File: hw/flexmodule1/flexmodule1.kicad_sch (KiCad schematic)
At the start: 62 parts, among them J1 AudioJack2, J2 AudioJack2, J3 AudioJack2, J4 AudioJack2, J5 AudioJack2, J6 rack_power, J7 SWD, J8 USB_B_Micro, J9 jack, SW1 mode, SW2 bootloader, U1 STM32G431K6Tx, U2 ADP7142AUJZ-5.0, U4 ADP7142AUJZ-3.3, U6 74HCT541, Y1 Crystal

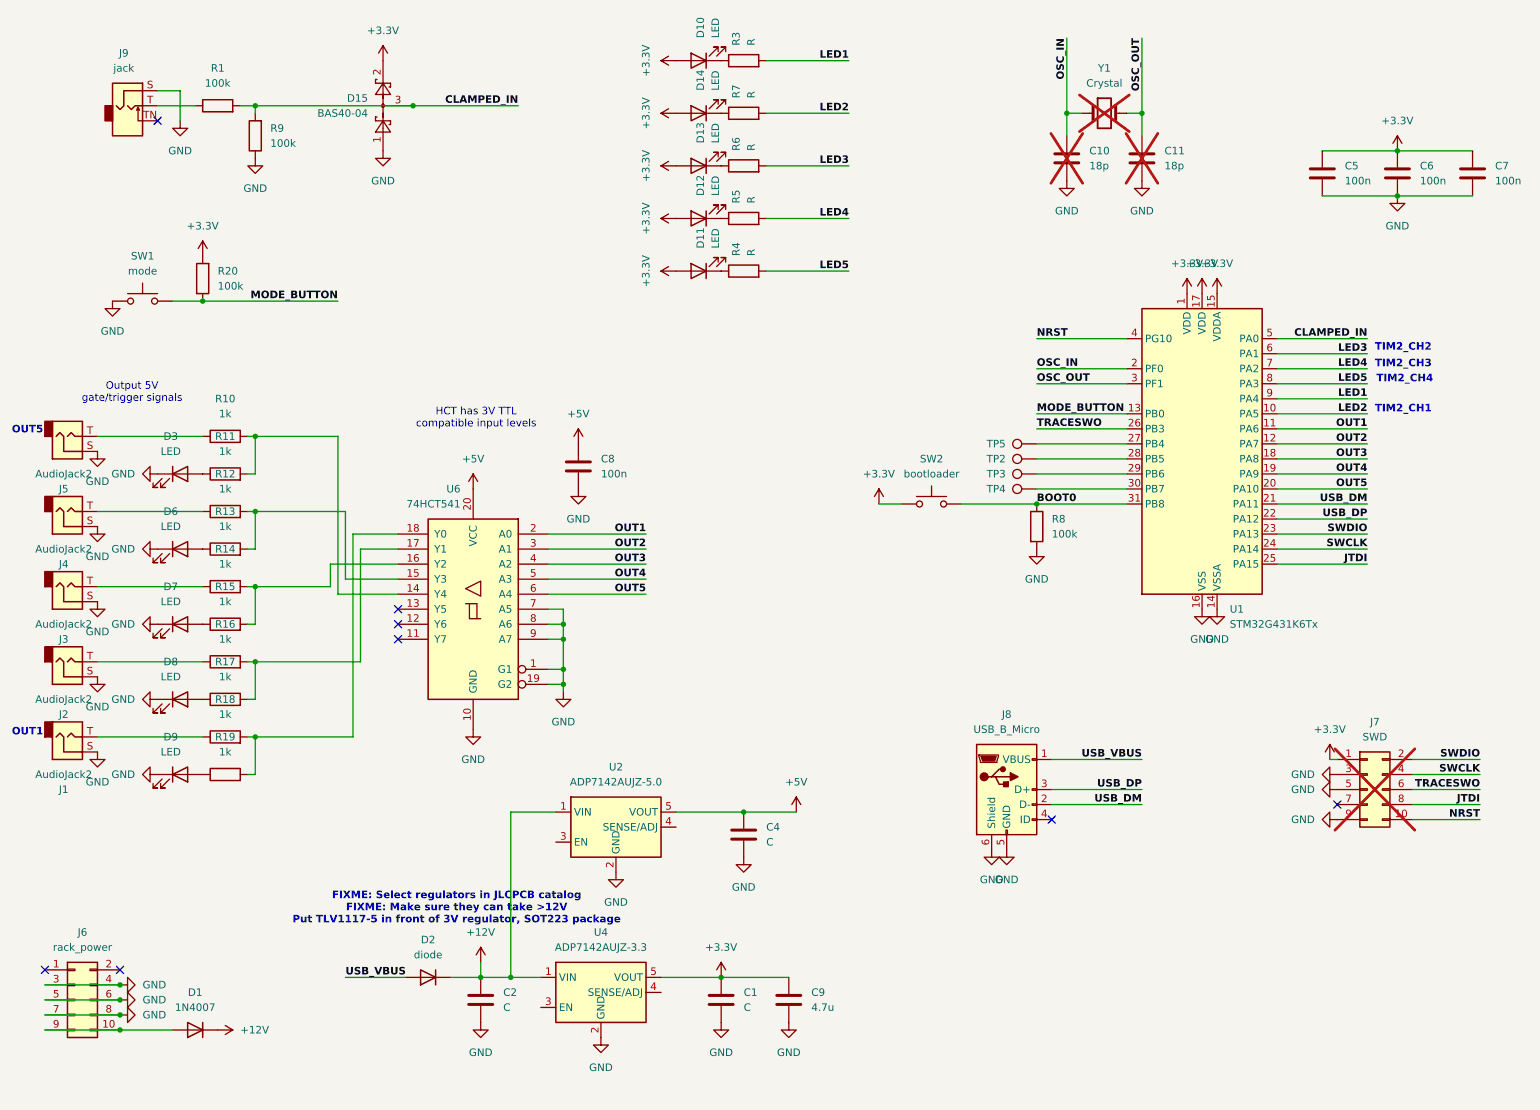
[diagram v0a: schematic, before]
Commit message: Change to a bigger LDO
Use a bigger 5V regulator with 12V input tolerance, so it might be
able to dissipate more heat. Not sure how warm this is going to get.
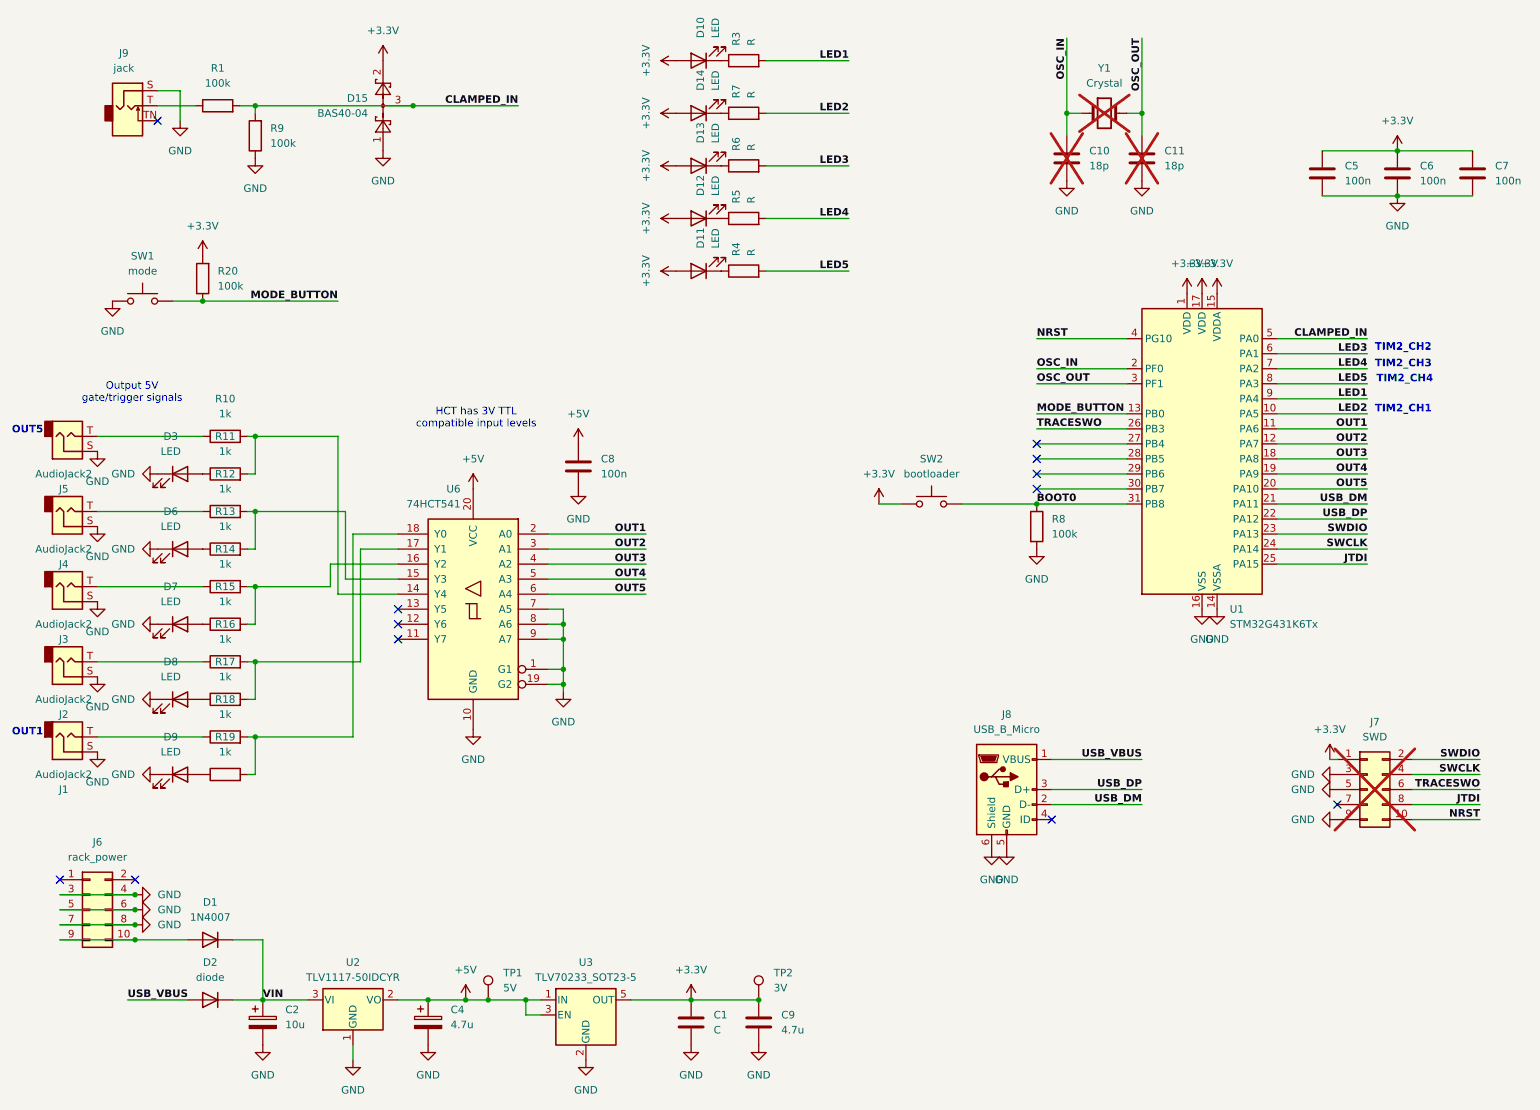
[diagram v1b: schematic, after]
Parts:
- removed TP3, TP4, TP5: tp, Holes:TP_0.9mm, symbol Connector:TestPoint
- removed U2: ADP7142AUJZ-5.0, Package_TO_SOT_SMD:TSOT-23-5, symbol Regulator_Linear:ADP7142AUJZ-5.0
- removed U4: ADP7142AUJZ-3.3, Package_TO_SOT_SMD:TSOT-23-5, symbol Regulator_Linear:ADP7142AUJZ-3.3
- added TP1: 5V, Holes:TP_0.9mm, symbol Connector:TestPoint
- added U2: TLV1117-50IDCYR, Package_TO_SOT_SMD:SOT-223-3_TabPin2, symbol Regulator_Linear:TLV1117-50
- added U3: TLV70233_SOT23-5, Package_TO_SOT_SMD:SOT-23-5, symbol Regulator_Linear:TLV70233_SOT23-5
- C2: value C -> 10u; footprint Capacitor_SMD:C_0603_1608Metric_Pad1.08x0.95mm_HandSolder -> Capacitor_THT:CP_Radial_D5.0mm_P2.50mm; symbol Device:C -> Device:C_Polarized
- C4: value C -> 4.7u; footprint Capacitor_SMD:C_0603_1608Metric_Pad1.08x0.95mm_HandSolder -> Capacitor_SMD:C_1206_3216Metric_Pad1.33x1.80mm_HandSolder; symbol Device:C -> Device:C_Polarized
- SW2: footprint Button_Switch_THT:SW_PUSH_6mm -> Button_Switch_SMD:SW_SPST_B3S-1000
- TP2: value tp -> 3V
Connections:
- net +3.3V: now also TP2.1, U3.5 (OUT)
- net +5V: now also TP1.1, U2.2 (VO), U3.1 (IN), U3.3 (EN)
- net GND: now also U2.1 (GND), U3.2 (GND)
- net at U1.28 (PB5): no longer TP2.1
- net +12V renamed VIN
- net VIN: now also U2.3 (VI)
- no-connect marks 8 -> 12
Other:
- note removed: "FIXME: Select regulators in JLCPCB catalog FIXME: Make sure they can take >12V Put TLV1117-5 in front of 3V regulator, SOT223 package"
- moved on the sheet: C1, C9, D1, D2, J6
